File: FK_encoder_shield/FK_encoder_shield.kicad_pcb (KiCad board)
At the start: 2 copper layers, 31.2 x 22.5 mm, 5 parts, among them J1 molex-35363-0660, J2 Conn_01x05_Female

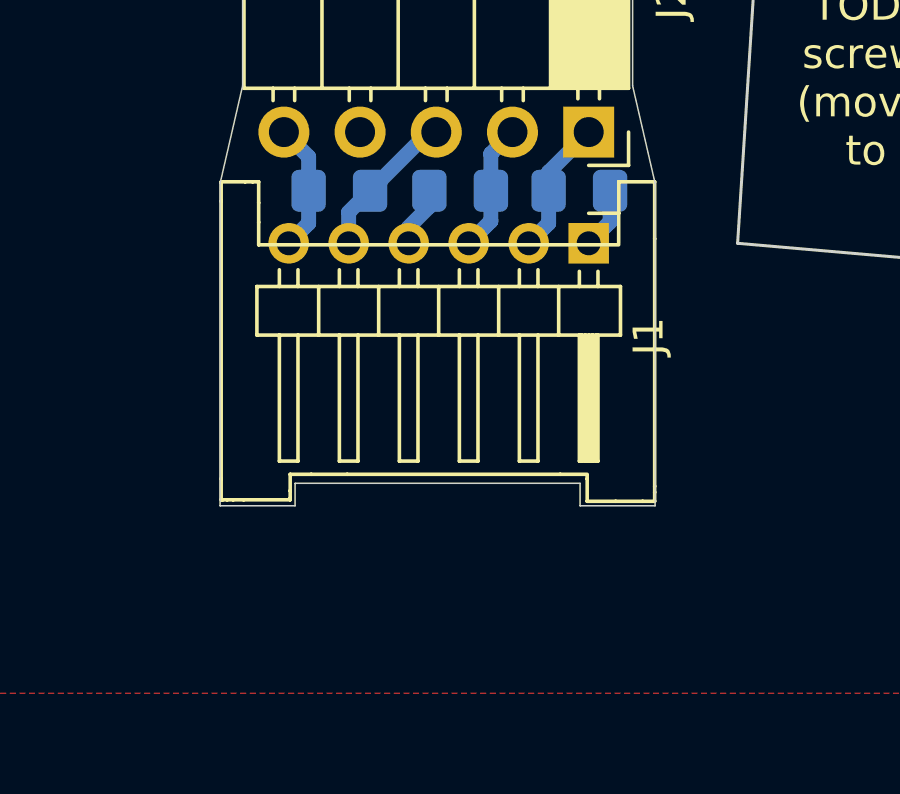
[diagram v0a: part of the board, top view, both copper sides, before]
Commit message: change connector to microclasp 4 wire
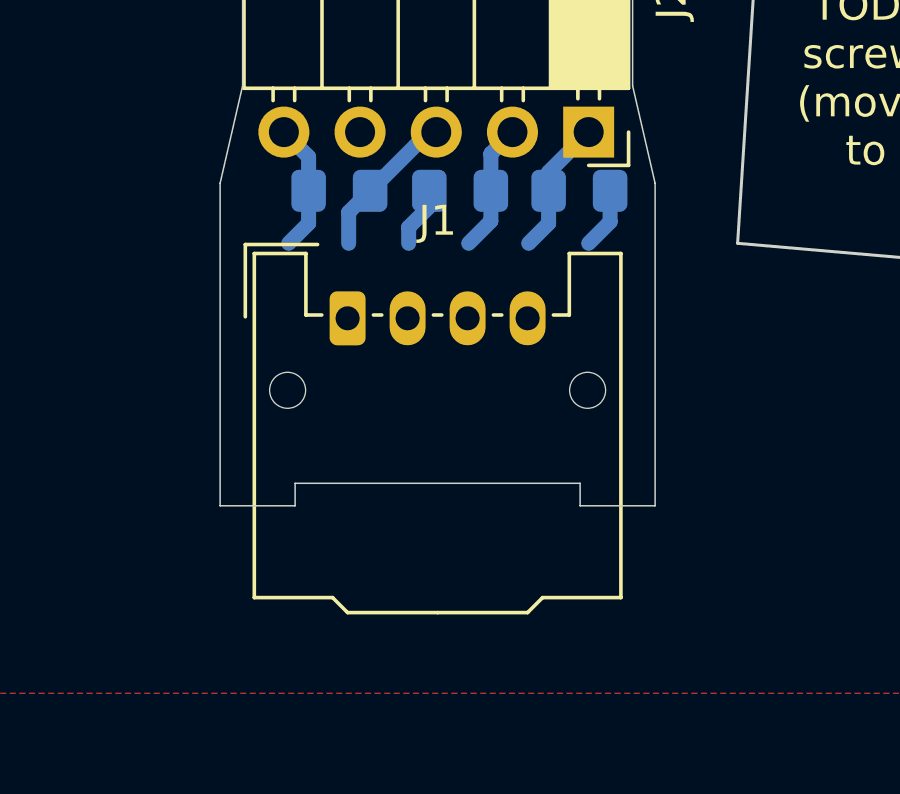
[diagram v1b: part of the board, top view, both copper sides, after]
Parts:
- J1: value molex-35363-0660 -> molex-51382-0400-microclasp; footprint FK_connectors:molex-35363-0660 -> FK_connectors:Molex_MicroClasp_55935-0410_1x04_P2.00mm_Horizontal_3DMODEL
- moved J1 8.42 mm to (150.5, 89.5), turned to 0 degrees
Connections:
- net /VCC renamed /5V
- J1 pad 2: /channel_B -> /A
- J1 pad 4: /GND -> /B
- J2 pad 1: /channel_B -> /B
- J2 pad 3: /channel_A -> /A
- R1 pad 1: /channel_B -> /B
- R2 pad 1: /channel_A -> /A
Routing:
- net /channel_A: track 5.06 -> 0.00 mm
- net /A: track 0.00 -> 5.06 mm
- net /channel_B: track 4.54 -> 0.00 mm
- net /B: track 0.00 -> 4.54 mm
